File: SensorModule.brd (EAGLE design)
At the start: 31.4 x 30.5 mm, 13 parts, among them U1 MPL3115A2LGA8, U2 ADXL345PATRICK

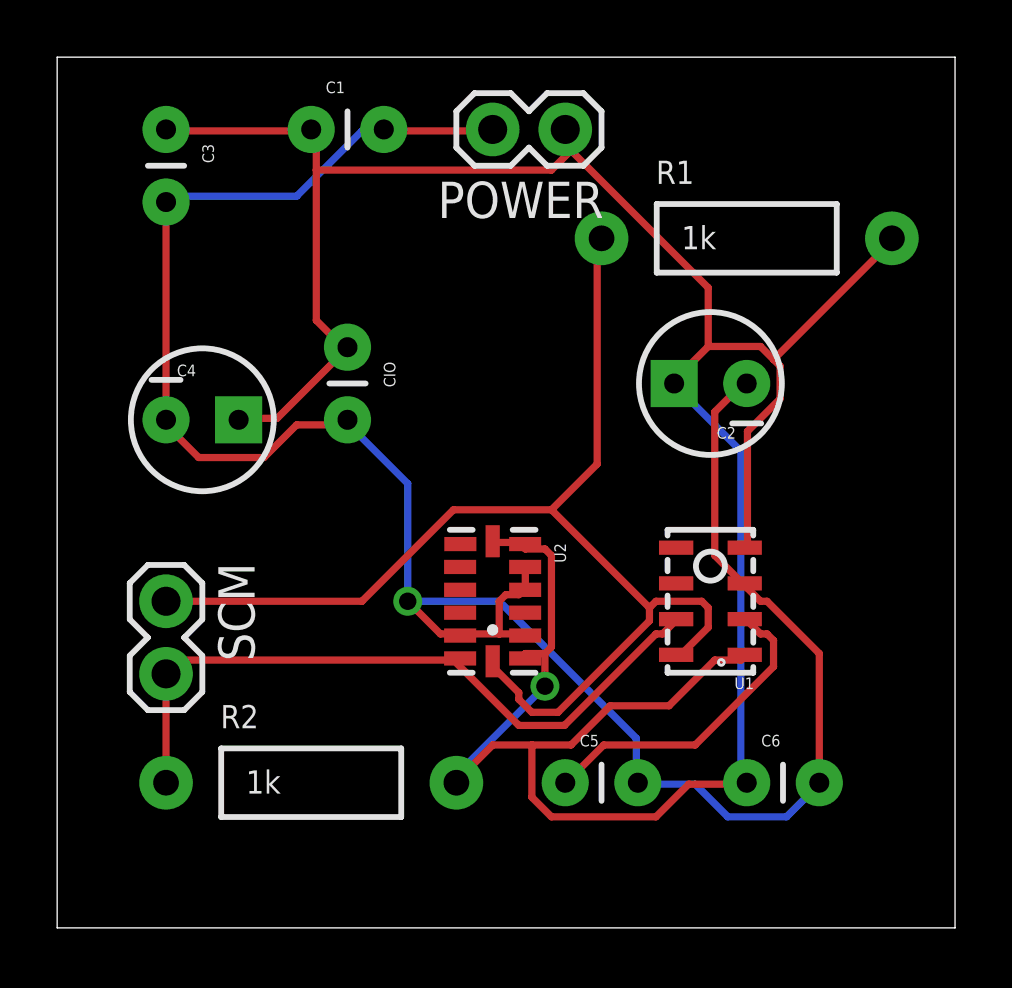
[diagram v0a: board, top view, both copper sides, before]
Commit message: fixed label sizes, renamed files
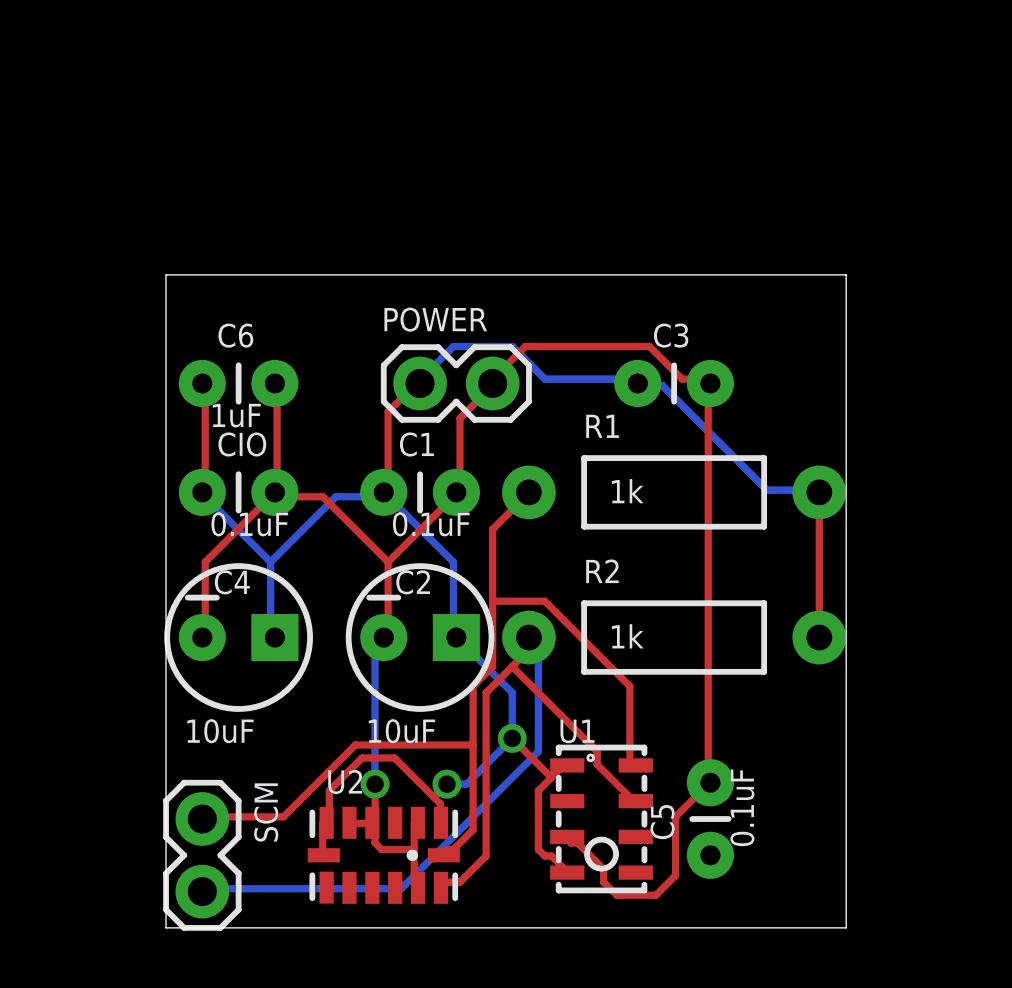
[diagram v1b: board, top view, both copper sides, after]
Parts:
- moved C6 23.6 mm to (1.27, 19.1)
- moved C3 18.8 mm to (16.5, 19.1), turned to 0 degrees
- moved R2 13.7 mm to (17.8, 10.2)
- moved C2 13.5 mm to (8.89, 10.2), turned to 0 degrees
- moved C1 13.0 mm to (7.62, 15.2)
- moved POWER 10.2 mm to (8.89, 19.1), turned to 0 degrees
- moved U2 9.67 mm to (7.62, 2.54), turned to 0 degrees
- moved R1 9.25 mm to (17.8, 15.2)
- moved U1 8.52 mm to (15.2, 3.81), turned to 0 degrees
- moved C4 7.73 mm to (2.54, 10.2)
- moved SCM 7.73 mm to (1.27, 3.81)
- moved CIO 7.18 mm to (1.27, 15.2), turned to 0 degrees
- moved C5 5.68 mm to (19.1, 2.54), turned to 90 degrees
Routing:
- net VCC_3.3V: track 105.1 -> 70.2 mm, vias 1 -> 2
- net N$1: track 11.2 -> 0.00 mm
- net SDA: track 24.9 -> 34.8 mm
- net SCL: track 42.6 -> 33.6 mm
- net GND: track 77.7 -> 69.4 mm
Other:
- board size 31.4 x 30.5 mm -> 23.8 x 22.9 mm
